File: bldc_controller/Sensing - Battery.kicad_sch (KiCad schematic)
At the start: 3 parts

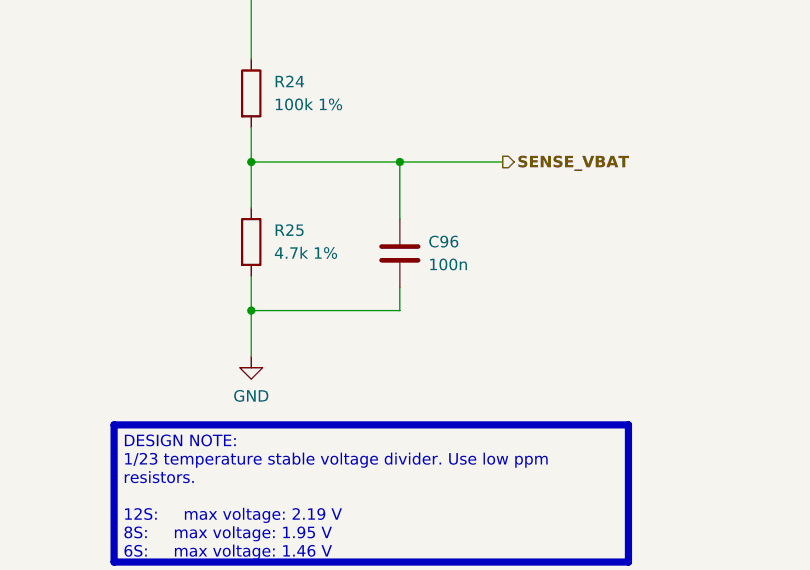
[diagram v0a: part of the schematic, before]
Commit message: schematic is complete. Replaced 5V buck and added pi filters.
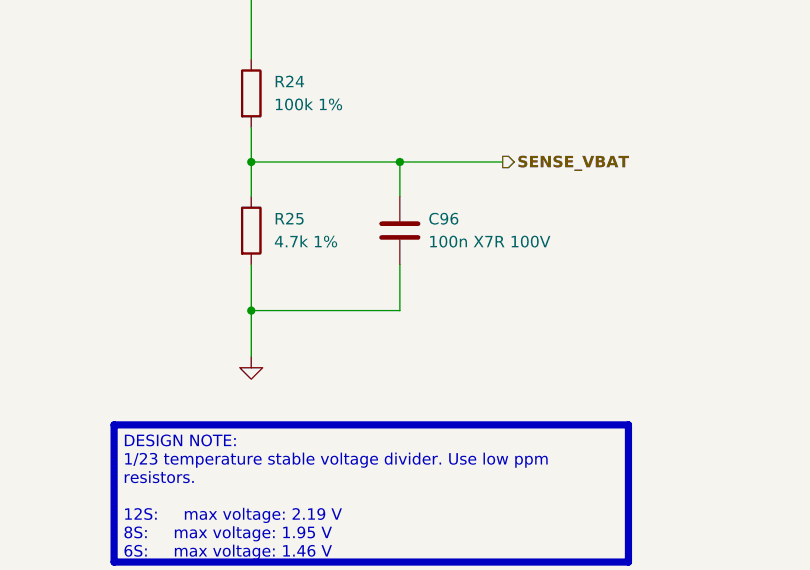
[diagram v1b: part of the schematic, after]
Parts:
- C96: value 100n -> 100n X7R 100V
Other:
- moved on the sheet: C96, R25
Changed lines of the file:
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@@
   (junction (at 134.62 87.63) (diameter 0) (color 0 0 0 0)
   )
-  (wire (pts (xy 151.13 71.12) (xy 151.13 77.47))
+  (wire (pts (xy 151.13 71.12) (xy 151.13 74.93))
     (stroke (width 0) (type default))
   )
@@
     (stroke (width 0) (type default))
   )
-  (wire (pts (xy 151.13 85.09) (xy 151.13 87.63))
+  (wire (pts (xy 151.13 82.55) (xy 151.13 87.63))
     (stroke (width 0) (type default))
   )
-  (wire (pts (xy 134.62 71.12) (xy 134.62 76.2))
+  (wire (pts (xy 134.62 71.12) (xy 134.62 74.93))
     (stroke (width 0) (type default))
   )
@@
     (stroke (width 0) (type default))
   )
-  (wire (pts (xy 134.62 87.63) (xy 134.62 83.82))
+  (wire (pts (xy 134.62 87.63) (xy 134.62 82.55))
     (stroke (width 0) (type default))
   )
@@
     (effects (font (face "Arial") (size 1.27 1.27) bold) (justify left))
   )
-  (symbol (lib_id "Device:R") (at 134.62 80.01 0) (unit 1)
+  (symbol (lib_id "Device:R") (at 134.62 78.74 0) (unit 1)
     (in_bom yes) (on_board yes) (dnp no) (fields_autoplaced)
-    (property "Reference" "R25" (at 137.16 78.74 0)
+    (property "Reference" "R25" (at 137.16 77.47 0)
       (effects (font (size 1.27 1.27)) (justify left))
     )
-    (property "Value" "4.7k 1%" (at 137.16 81.28 0)
+    (property "Value" "4.7k 1%" (at 137.16 80.01 0)
       (effects (font (size 1.27 1.27)) (justify left))
     )
-    (property "Footprint" "0_resistor_smd:R_0402_1005_DensityHigh" (at 132.842 80.01 90)
+    (property "Footprint" "0_resistor_smd:R_0402_1005_DensityHigh" (at 132.842 78.74 90)
       (effects (font (size 1.27 1.27)) hide)
     )
-    (property "Datasheet" "~" (at 134.62 80.01 0)
+    (property "Datasheet" "~" (at 134.62 78.74 0)
       (effects (font (size 1.27 1.27)) hide)
     )
@@
     )
   )
-  (symbol (lib_id "Device:C") (at 151.13 81.28 0) (unit 1)
+  (symbol (lib_id "Device:C") (at 151.13 78.74 0) (unit 1)
     (in_bom yes) (on_board yes) (dnp no) (fields_autoplaced)
-    (property "Reference" "C96" (at 154.305 80.01 0)
+    (property "Reference" "C96" (at 154.305 77.47 0)
       (effects (font (size 1.27 1.27)) (justify left))
     )
-    (property "Value" "100n" (at 154.305 82.55 0)
+    (property "Value" "100n X7R 100V" (at 154.305 80.01 0)
       (effects (font (size 1.27 1.27)) (justify left))
     )
-    (property "Footprint" "0_capacitor_smd:C_0402_1005_DensityHigh" (at 152.0952 85.09 0)
+    (property "Footprint" "0_capacitor_smd:C_0402_1005_DensityHigh" (at 152.0952 82.55 0)
       (effects (font (size 1.27 1.27)) hide)
     )
-    (property "Datasheet" "~" (at 151.13 81.28 0)
+    (property "Datasheet" "~" (at 151.13 78.74 0)
       (effects (font (size 1.27 1.27)) hide)
     )
@@
     )
     (property "Value" "GND" (at 134.62 97.155 0)
-      (effects (font (size 1.27 1.27)))
+      (effects (font (size 1.27 1.27)) hide)
     )
     (property "Footprint" "" (at 134.62 92.71 0)
